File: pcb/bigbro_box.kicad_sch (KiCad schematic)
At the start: 48 parts, among them J1 Current Sense, J2 Display, J3 Mains, J4 Debug, J5 RFID, J6 Relay, J7 Ext, K1 G5LE-1, Q1 MMBT3904, Q2 MMBT3904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

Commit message: Use a smaller fuse.
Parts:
- F1: footprint modules:Fuseholder5x20_horiz_SemiClosed_Casing10x25mm -> Fuse:Fuse_Littelfuse_395Series
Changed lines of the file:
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@@
 			)
 		)
-		(property "Footprint" "modules:Fuseholder5x20_horiz_SemiClosed_Casing10x25mm"
+		(property "Footprint" "Fuse:Fuse_Littelfuse_395Series"
 			(at 330.2 39.37 0)
 			(effects

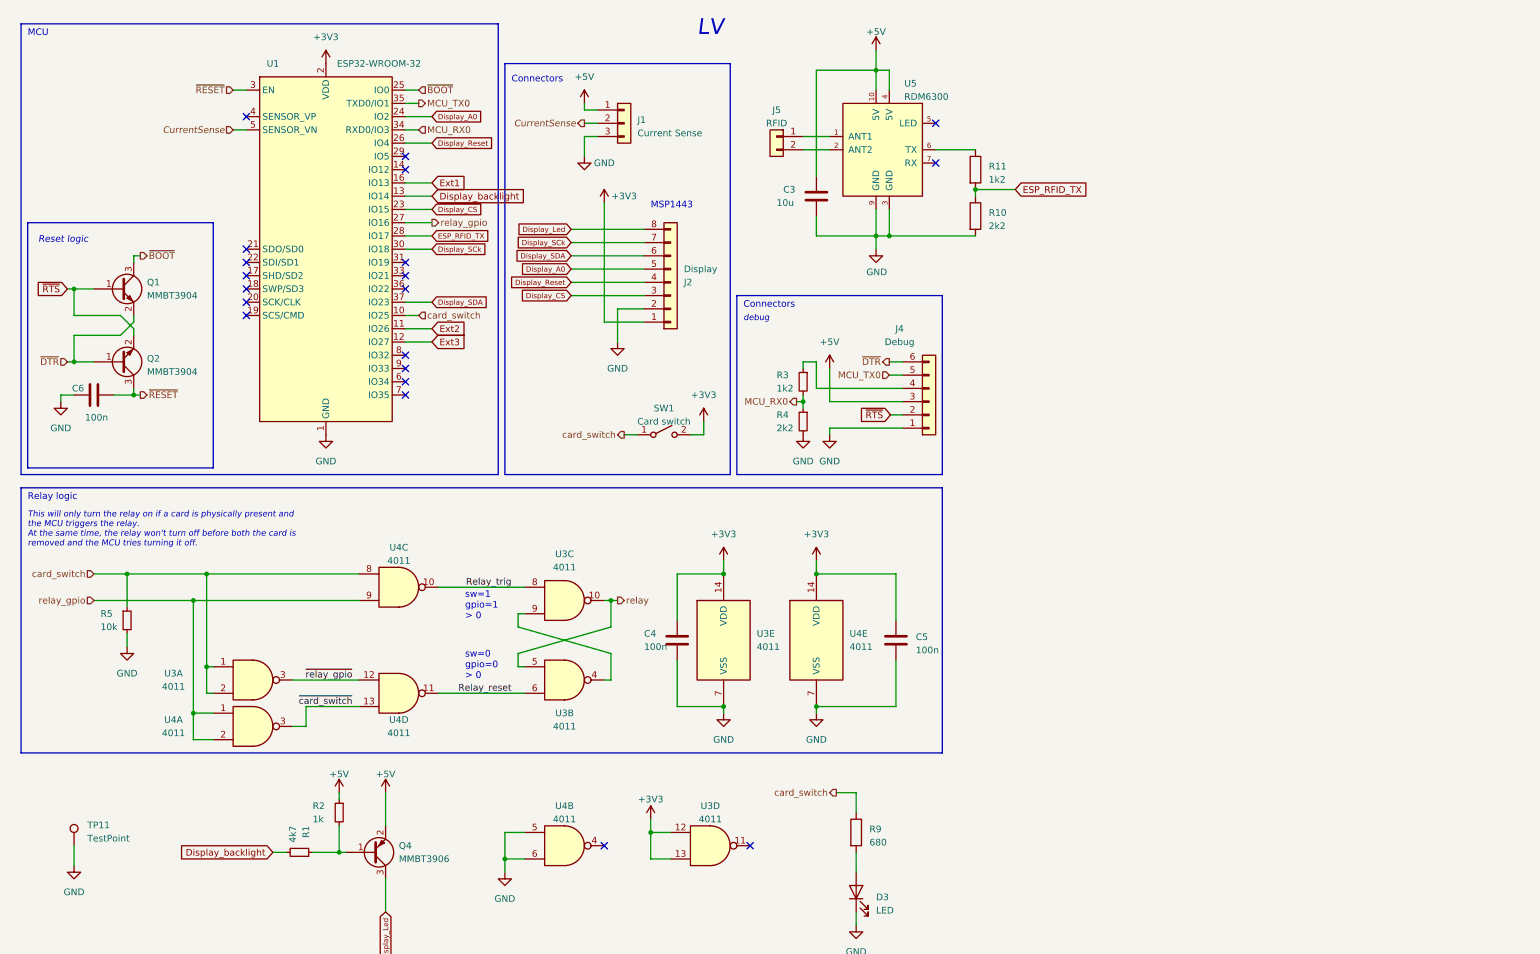
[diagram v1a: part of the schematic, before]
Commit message: Add extra transistor.
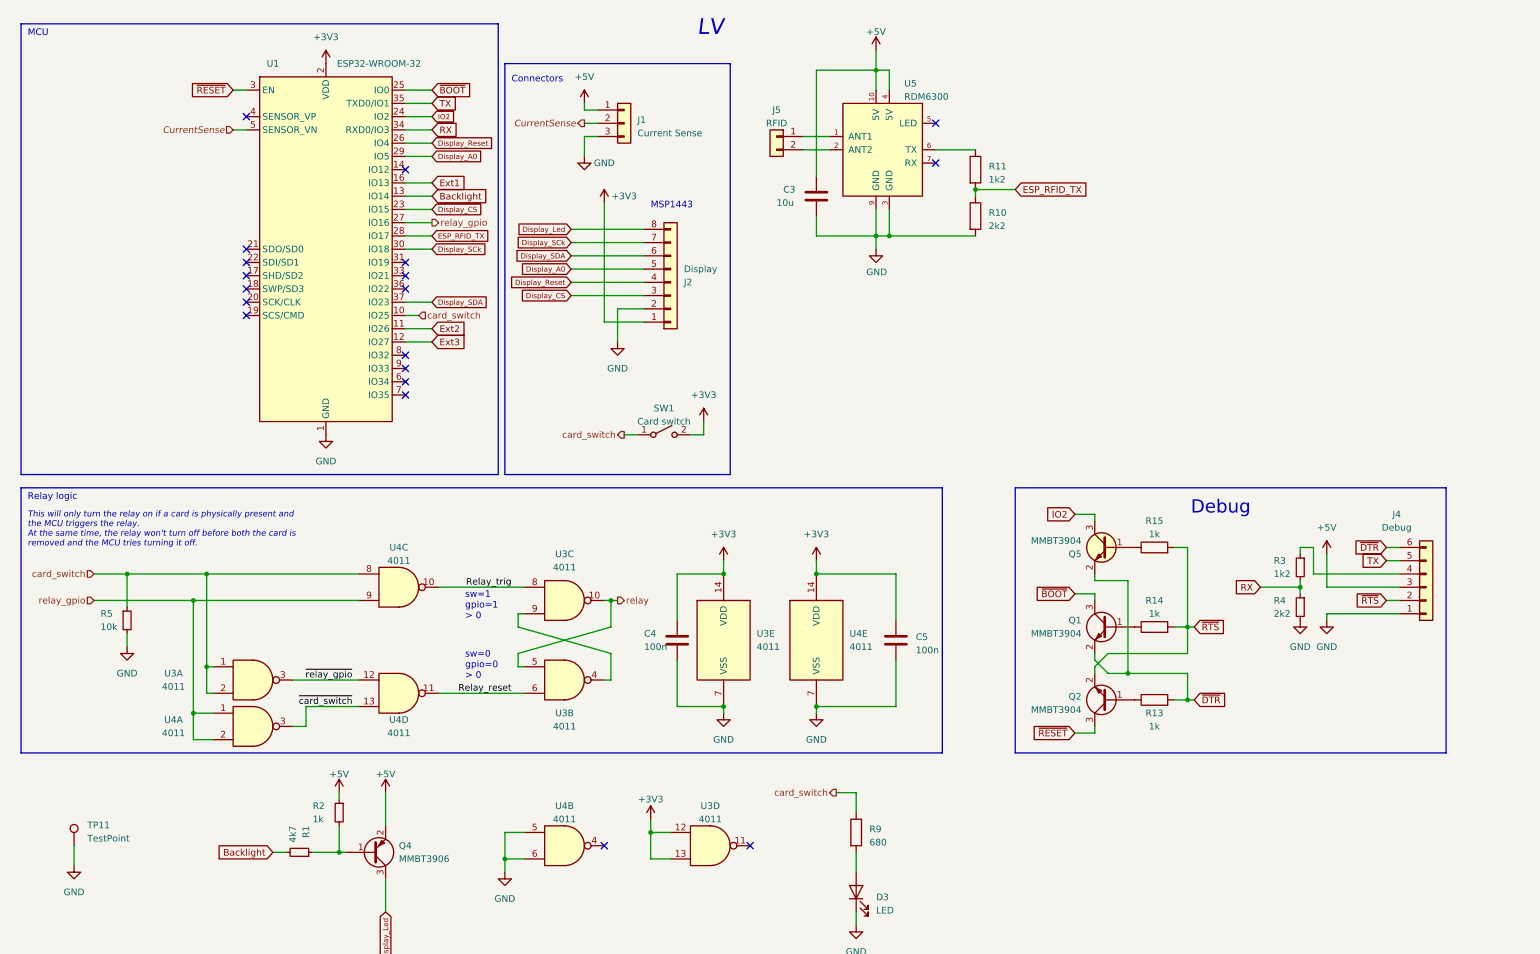
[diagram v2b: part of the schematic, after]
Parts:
- removed C6: 100n, Capacitor_SMD:C_0603_1608Metric, symbol Device:C
- added Q5: MMBT3904, PCM_Package_TO_SOT_SMD_AKL:SOT-23, symbol PCM_Transistor_BJT_AKL:MMBT3904
- added R13, R14, R15: 1k, PCM_Resistor_SMD_AKL:R_0603_1608Metric, symbol Device:R
- C1, C3, C4, C5: footprint Capacitor_SMD:C_0603_1608Metric -> PCM_Capacitor_SMD_AKL:C_0603_1608Metric
- C2: footprint Capacitor_SMD:C_0603_1608Metric_Pad1.08x0.95mm_HandSolder -> PCM_Capacitor_SMD_AKL:C_0603_1608Metric
- D2, D3: footprint LED_SMD:LED_0603_1608Metric -> PCM_LED_SMD_AKL:LED_0603_1608Metric
- Q1, Q2, Q3, Q4: footprint Package_TO_SOT_SMD:SOT-23 -> PCM_Package_TO_SOT_SMD_AKL:SOT-23
- R1, R10, R11, R12, R2, R3, R4, R5, R6, R7, R8, R9: footprint Resistor_SMD:R_0603_1608Metric -> PCM_Resistor_SMD_AKL:R_0603_1608Metric
- U2: footprint Package_TO_SOT_SMD:SOT-223-3_TabPin2 -> PCM_Package_TO_SOT_SMD_AKL:SOT-223-3_TabPin2
- U3, U4: footprint Package_SO:SOIC-14_3.9x8.7mm_P1.27mm -> PCM_Package_SO_AKL:SOIC-14_3.9x8.7mm_P1.27mm
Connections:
- net Display_A0: now also U1.29 (IO5); no longer U1.24 (IO2)
- net ~{DTR}: now also Q5.2 (E), R13.2; no longer Q2.1 (B)
- net ~{RTS}: now also R14.2, R15.2; no longer Q1.1 (B)
- net Display_backlight renamed Backlight
- net MCU_RX0 renamed RX
- net MCU_TX0 renamed TX
- new net: Q2.1 (B), R13.1
- new net: Q1.1 (B), R14.1
- new net: Q5.1 (B), R15.1
- new net IO2: Q5.3 (C), U1.24 (IO2)
- no-connect marks 20 -> 19
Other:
- note added: "Debug"
- note removed: "Reset logic"
- note removed: "debug"
- moved on the sheet: J4, Q1, Q2, R3, R4

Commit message: Route.
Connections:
- net SENSE: now reaches U1.6 (IO34)
- net SENSE: now also J1.2 (Pin_2)
- net CurrentSense: no longer names the net of U1.5 (SENSOR_VN)
- net CurrentSense: no longer J1.2 (Pin_2)
- net card_switch renamed SW
- net relay renamed RELAY
- net relay_gpio renamed RELAY_EN
- net ~{card_switch}: no longer names the net of U4.13, U4.3
- net ~{relay_gpio}: no longer names the net of U3.3, U4.12
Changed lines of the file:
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@@
 	)
 	(no_connect
-		(at 88.9 85.09)
-	)
-	(no_connect
 		(at 88.9 80.01)
 	)
@@
 	)
 	(no_connect
+		(at 58.42 36.83)
+	)
+	(no_connect
 		(at 88.9 44.45)
 	)
@@
 	(wire
 		(pts
-			(xy 55.88 36.83) (xy 58.42 36.83)
-		)
-		(stroke
-			(width 0)
-			(type default)
-		)
-	)
-	(wire
-		(pts
 			(xy 50.8 121.92) (xy 50.8 139.7)
 		)
@@
 	(wire
 		(pts
-			(xy 88.9 72.39) (xy 91.44 72.39)
+			(xy 88.9 72.39) (xy 93.98 72.39)
 		)
 		(stroke
@@
 	(wire
 		(pts
+			(xy 88.9 85.09) (xy 93.98 85.09)
+		)
+		(stroke
+			(width 0)
+			(type default)
+		)
+	)
+	(wire
+		(pts
 			(xy 367.03 40.64) (xy 367.03 39.37)
 		)
@@
 		)
 	)
-	(label "~{card_switch}"
-		(at 78.74 147.32 180)
-		(effects
-			(font
-				(size 1.27 1.27)
-			)
-			(justify right bottom)
-		)
-	)
 	(label "NC"
 		(at 349.25 69.85 270)
@@
 		)
 	)
-	(label "~{relay_gpio}"
-		(at 78.74 142.24 180)
-		(effects
-			(font
-				(size 1.27 1.27)
-			)
-			(justify right bottom)
-		)
-	)
 	(label "NC"
 		(at 369.57 81.28 180)
@@
 		)
 	)
+	(global_label "RELAY"
+		(shape input)
+		(at 129.54 127 0)
+		(fields_autoplaced yes)
+		(effects
+			(font
+				(size 1.27 1.27)
+			)
+			(justify left)
+		)
+		(property "Intersheetrefs" "${INTERSHEET_REFS}"
+			(at 138.1495 127 0)
+			(effects
+				(font
+					(size 1.27 1.27)
+				)
+				(justify left)
+				(hide yes)
+			)
+		)
+	)
 	(global_label "Ext2"
 		(shape input)
@@
 		)
 	)
+	(global_label "SENSE"
+		(shape input)
+		(at 123.19 35.56 180)
+		(fields_autoplaced yes)
+		(effects
+			(font
+				(size 1.27 1.27)
+			)
+			(justify right)
+		)
+		(property "Intersheetrefs" "${INTERSHEET_REFS}"
+			(at 114.1573 35.56 0)
+			(effects
+				(font
+					(size 1.27 1.27)
+				)
+				(justify right)
+				(hide yes)
+			)
+		)
+	)
 	(global_label "Display_A0"
 		(shape input)
@@
 		)
 	)
+	(global_label "SW"
+		(shape input)
+		(at 29.21 121.92 180)
+		(fields_autoplaced yes)
+		(effects
+			(font
+				(size 1.27 1.27)
+			)
+			(justify right)
+		)
+		(property "Intersheetrefs" "${INTERSHEET_REFS}"
+			(at 23.5639 121.92 0)
+			(effects
+				(font
+					(size 1.27 1.27)
+				)
+				(justify right)
+				(hide yes)
+			)
+		)
+	)
 	(global_label "Display_CS"
 		(shape input)
@@
 		)
 	)
+	(global_label "RELAY_EN"
+		(shape input)
+		(at 93.98 54.61 0)
+		(fields_autoplaced yes)
+		(effects
+			(font
+				(size 1.27 1.27)
+			)
+			(justify left)
+		)
+		(property "Intersheetrefs" "${INTERSHEET_REFS}"
+			(at 106.0366 54.61 0)
+			(effects
+				(font
+					(size 1.27 1.27)
+				)
+				(justify left)
+				(hide yes)
+			)
+		)
+	)
 	(global_label "TX"
 		(shape input)
@@
 		)
 	)
+	(global_label "RELAY"
+		(shape input)
+		(at 322.58 101.6 180)
+		(fields_autoplaced yes)
+		(effects
+			(font
+				(size 1.27 1.27)
+			)
+			(justify right)
+		)
+		(property "Intersheetrefs" "${INTERSHEET_REFS}"
+			(at 313.9705 101.6 0)
+			(effects
+				(font
+					(size 1.27 1.27)
+				)
+				(justify right)
+				(hide yes)
+			)
+		)
+	)
 	(global_label "ESP_RFID_TX"
 		(shape input)
@@
 		)
 	)
+	(global_label "SW"
+		(shape input)
+		(at 171.45 163.83 180)
+		(fields_autoplaced yes)
+		(effects
+			(font
+				(size 1.27 1.27)
+			)
+			(justify right)
+		)
+		(property "Intersheetrefs" "${INTERSHEET_REFS}"
+			(at 165.8039 163.83 0)
+			(effects
+				(font
+					(size 1.27 1.27)
+				)
+				(justify right)
+				(hide yes)
+			)
+		)
+	)
 	(global_label "~{BOOT}"
 		(shape input)
@@
 		)
 	)
+	(global_label "SW"
+		(shape input)
+		(at 93.98 72.39 0)
+		(fields_autoplaced yes)
+		(effects
+			(font
+				(size 1.27 1.27)
+			)
+			(justify left)
+		)
+		(property "Intersheetrefs" "${INTERSHEET_REFS}"
+			(at 99.6261 72.39 0)
+			(effects
+				(font
+					(size 1.27 1.27)
+				)
+				(justify left)
+				(hide yes)
+			)
+		)
+	)
 	(global_label "IO2"
 		(shape input)
@@
 		)
 	)
+	(global_label "SW"
+		(shape input)
+		(at 130.81 95.25 180)
+		(fields_autoplaced yes)
+		(effects
+			(font
+				(size 1.27 1.27)
+			)
+			(justify right)
+		)
+		(property "Intersheetrefs" "${INTERSHEET_REFS}"
+			(at 125.1639 95.25 0)
+			(effects
+				(font
+					(size 1.27 1.27)
+				)
+				(justify right)
+				(hide yes)
+			)
+		)
+	)
+	(global_label "SENSE"
+		(shape input)
+		(at 93.98 85.09 0)
+		(fields_autoplaced yes)
+		(effects
+			(font
+				(size 1.27 1.27)
+			)
+			(justify left)
+		)
+		(property "Intersheetrefs" "${INTERSHEET_REFS}"
+			(at 103.0127 85.09 0)
+			(effects
+				(font
+					(size 1.27 1.27)
+				)
+				(justify left)
+				(hide yes)
+			)
+		)
+	)
 	(global_label "Ext1"
 		(shape input)
@@
 		)
 	)
+	(global_label "RELAY_EN"
+		(shape input)
+		(at 29.21 127 180)
+		(fields_autoplaced yes)
+		(effects
+			(font
+				(size 1.27 1.27)
+			)
+			(justify right)
+		)
+		(property "Intersheetrefs" "${INTERSHEET_REFS}"
+			(at 17.1534 127 0)
+			(effects
+				(font
+					(size 1.27 1.27)
+				)
+				(justify right)
+				(hide yes)
+			)
+		)
+	)
 	(global_label "Display_SCk"
 		(shape input)
@@
 		)
 	)
-	(hierarchical_label "relay"
-		(shape input)
-		(at 322.58 101.6 180)
-		(effects
-			(font
-				(size 1.27 1.27)
-			)
-			(justify right)
-		)
-	)
-	(hierarchical_label "relay_gpio"
-		(shape input)
-		(at 29.21 127 180)
-		(effects
-			(font
-				(size 1.27 1.27)
-			)
-			(justify right)
-		)
-	)
-	(hierarchical_label "card_switch"
-		(shape output)
-		(at 130.81 95.25 180)
-		(effects
-			(font
-				(size 1.27 1.27)
-			)
-			(justify right)
-		)
-	)
-	(hierarchical_label "relay_gpio"
-		(shape output)
-		(at 93.98 54.61 0)
-		(effects
-			(font
-				(size 1.27 1.27)
-			)
-			(justify left)
-		)
-	)
-	(hierarchical_label "card_switch"
-		(shape input)
-		(at 29.21 121.92 180)
-		(effects
-			(font
-				(size 1.27 1.27)
-			)
-			(justify right)
-		)
-	)
-	(hierarchical_label "CurrentSense"
-		(shape output)
-		(at 123.19 35.56 180)
-		(effects
-			(font
-				(size 1.27 1.27)
-				(italic yes)
-			)
-			(justify right)
-		)
-	)
-	(hierarchical_label "CurrentSense"
-		(shape input)
-		(at 55.88 36.83 180)
-		(effects
-			(font
-				(size 1.27 1.27)
-				(italic yes)
-			)
-			(justify right)
-		)
-	)
 	(hierarchical_label "~{BOOT}"
 		(shape input)
@@
 		)
 	)
-	(hierarchical_label "relay"
-		(shape output)
-		(at 129.54 127 0)
-		(effects
-			(font
-				(size 1.27 1.27)
-			)
-			(justify left)
-		)
-	)
-	(hierarchical_label "card_switch"
-		(shape output)
-		(at 171.45 163.83 180)
-		(effects
-			(font
-				(size 1.27 1.27)
-			)
-			(justify right)
-		)
-	)
 	(hierarchical_label "~{RESET}"
 		(shape input)
@@
 		(effects
 			(font
-				(size 1.27 1.27)
-			)
-			(justify left)
-		)
-	)
-	(hierarchical_label "card_switch"
-		(shape input)
-		(at 91.44 72.39 0)
-		(effects
-			(font

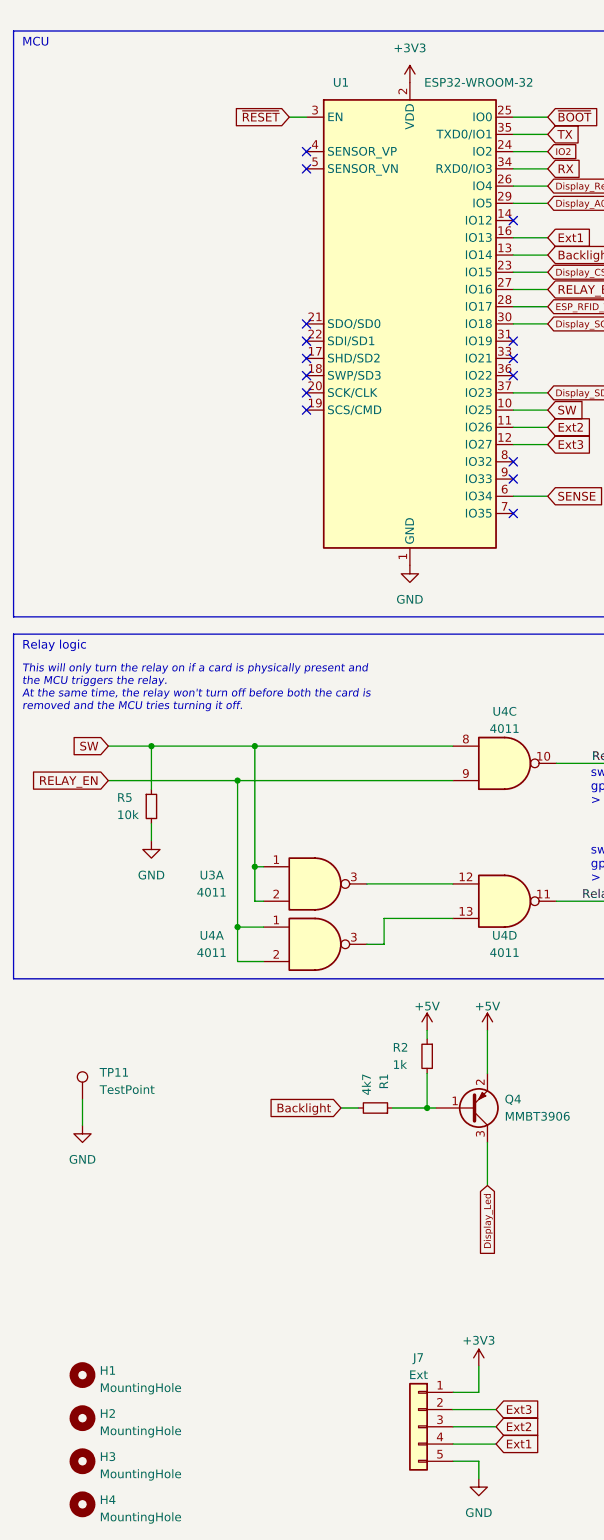
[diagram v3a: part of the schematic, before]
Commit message: Start adding JLCPCB part numbers.
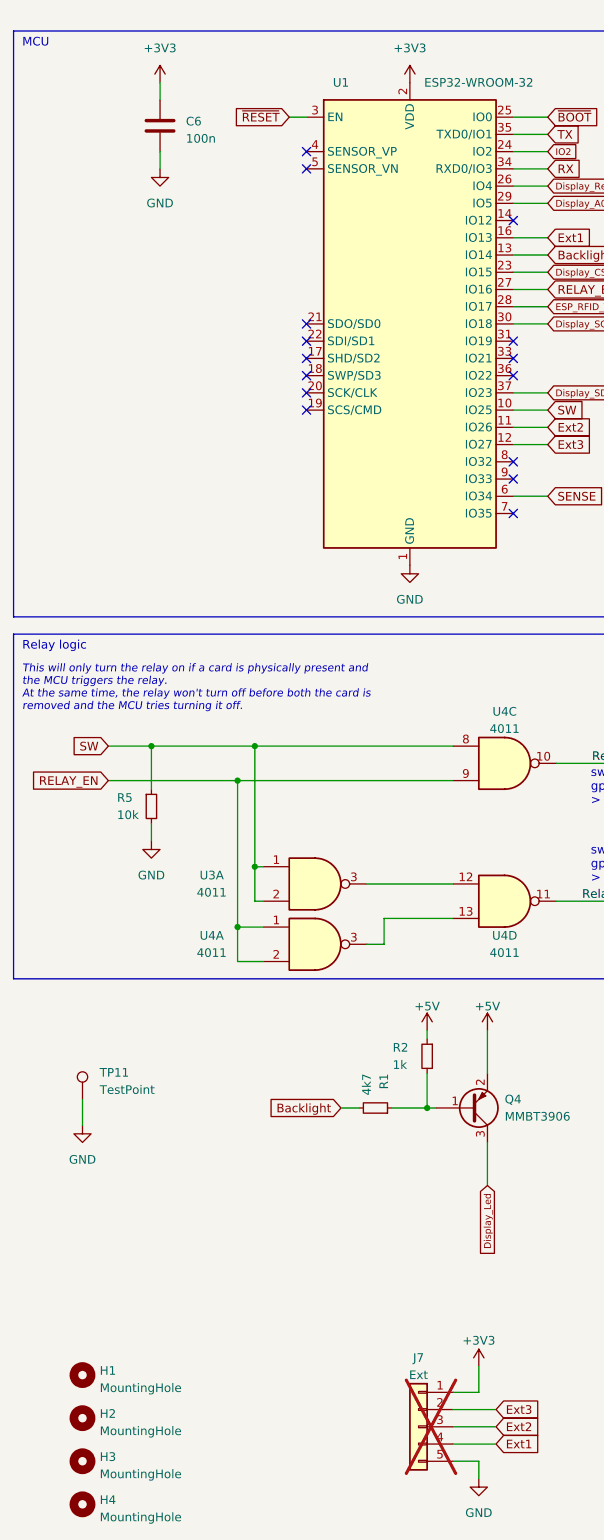
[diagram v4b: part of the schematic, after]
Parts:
- added C6: 100n, PCM_Capacitor_SMD_AKL:C_0603_1608Metric, symbol Device:C
- C1: LCSC (none) -> C15849
- C2: LCSC (none) -> C96446
- C4, C5: LCSC (none) -> C14663
- J1: LCSC (none) -> C144394
- J4: LCSC (none) -> C37208
- J7: now not fitted
- R1: LCSC (none) -> C23162
- R13, R14, R15, R2, R7: LCSC (none) -> C14676
- R3: LCSC (none) -> C22765
- R4: LCSC (none) -> C5362360
- R5, R8: LCSC (none) -> C15401
- R6: LCSC (none) -> C22843
- U1: LCSC (none) -> C95209
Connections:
- net +3V3: now also C6.1
- net GND: now also C6.2
